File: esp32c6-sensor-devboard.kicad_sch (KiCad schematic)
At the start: 85 parts, among them J1 Conn_01x04_Pin, J2 Micro_SD_Card_Det1, J3 Screw_Terminal_01x02, J4 USB_C_Receptacle_USB2.0_14P, J5 Screw_Terminal_01x02, J6 Screw_Terminal_01x06, J7 Screw_Terminal_01x04, J8 Conn_01x04_Pin, J9 Conn_01x03_Pin, SW1 SW_Push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

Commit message: schem: assign footprints
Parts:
- AE1: footprint (none) -> RF_Antenna:Johanson_2450AT18x100
- C3: footprint (none) -> Capacitor_SMD:C_0603_1608Metric
- C48, C49, C50, C51: footprint (none) -> Capacitor_SMD:C_0402_1005Metric
- D10: footprint (none) -> LED_SMD:LED_0805_2012Metric
- D9: footprint (none) -> LED_SMD:LED_0603_1608Metric
- J1, J8: footprint (none) -> Connector_PinHeader_2.54mm:PinHeader_1x04_P2.54mm_Vertical
- J3, J5: footprint (none) -> TerminalBlock:TerminalBlock_Altech_AK300-2_P5.00mm
- J6: footprint (none) -> TerminalBlock_Phoenix:TerminalBlock_Phoenix_MKDS-1,5-6_1x06_P5.00mm_Horizontal
- J7: footprint (none) -> TerminalBlock:TerminalBlock_Altech_AK300-4_P5.00mm
- J9: footprint (none) -> Connector_PinHeader_2.54mm:PinHeader_1x03_P2.54mm_Vertical
- JP1: footprint (none) -> Connector_PinHeader_2.54mm:PinHeader_1x02_P2.54mm_Vertical
- R1, R2, R3, R4, R5, R57, R58, R59, R6, R60, R61, R62: footprint (none) -> Resistor_SMD:R_0603_1608Metric
- R10, R14, R16, R17, R18, R19, R20, R21, R22: footprint (none) -> Resistor_SMD:R_0402_1005Metric
- SW1, SW2: footprint Button_Switch_THT:SW_SPST_Omron_B3F-40xx -> Button_Switch_SMD:SW_SPST_TS-1088-xR020
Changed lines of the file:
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@@
 			)
 		)
-		(property "Footprint" ""
+		(property "Footprint" "TerminalBlock:TerminalBlock_Altech_AK300-2_P5.00mm"
 			(at 227.33 157.48 0)
 			(effects
@@
 			)
 		)
-		(property "Footprint" ""
+		(property "Footprint" "TerminalBlock:TerminalBlock_Altech_AK300-4_P5.00mm"
 			(at 275.59 143.51 0)
 			(effects
@@
 			)
 		)
-		(property "Footprint" ""
+		(property "Footprint" "Resistor_SMD:R_0603_1608Metric"
 			(at 48.26 97.028 90)
 			(effects
@@
 			)
 		)
-		(property "Footprint" ""
+		(property "Footprint" "Resistor_SMD:R_0603_1608Metric"
 			(at 222.25 99.568 90)
 			(effects
@@
 			)
 		)
-		(property "Footprint" ""
+		(property "Footprint" "Resistor_SMD:R_0603_1608Metric"
 			(at 270.002 27.94 90)
 			(effects
@@
 			)
 		)
-		(property "Footprint" ""
+		(property "Footprint" "Capacitor_SMD:C_0402_1005Metric"
 			(at 270.8148 69.85 0)
 			(effects
@@
 			)
 		)
-		(property "Footprint" ""
+		(property "Footprint" "Resistor_SMD:R_0402_1005Metric"
 			(at 135.89 148.082 90)
 			(effects
@@
 			)
 		)
-		(property "Footprint" ""
+		(property "Footprint" "Resistor_SMD:R_0603_1608Metric"
 			(at 222.25 94.488 90)
 			(effects
@@
 			)
 		)
-		(property "Footprint" "Button_Switch_THT:SW_SPST_Omron_B3F-40xx"
+		(property "Footprint" "Button_Switch_SMD:SW_SPST_TS-1088-xR020"
 			(at 26.67 180.34 0)
 			(effects
@@
 			)
 		)
-		(property "Footprint" ""
+		(property "Footprint" "Resistor_SMD:R_0603_1608Metric"
 			(at 48.26 107.188 90)
 			(effects
@@
 			)
 		)
-		(property "Footprint" ""
+		(property "Footprint" "Resistor_SMD:R_0402_1005Metric"
 			(at 135.89 145.542 90)
 			(effects
@@
 			)
 		)
-		(property "Footprint" ""
+		(property "Footprint" "Resistor_SMD:R_0402_1005Metric"
 			(at 143.51 65.532 90)
 			(effects
@@
 			)
 		)
-		(property "Footprint" ""
+		(property "Footprint" "Resistor_SMD:R_0603_1608Metric"
 			(at 246.38 83.058 90)
 			(effects
@@
 			)
 		)
-		(property "Footprint" ""
+		(property "Footprint" "Capacitor_SMD:C_0402_1005Metric"
 			(at 264.16 24.4348 0)
 			(effects
@@
 			)
 		)
-		(property "Footprint" ""
+		(property "Footprint" "Capacitor_SMD:C_0603_1608Metric"
 			(at 159.7152 165.1 0)
 			(effects
@@
 			)
 		)
-		(property "Footprint" ""
+		(property "Footprint" "Resistor_SMD:R_0603_1608Metric"
 			(at 154.432 132.08 90)
 			(effects
@@
 			)
 		)
-		(property "Footprint" ""
+		(property "Footprint" "Connector_PinHeader_2.54mm:PinHeader_1x03_P2.54mm_Vertical"
 			(at 63.5 118.11 0)
 			(effects
@@
 			)
 		)
-		(property "Footprint" ""
+		(property "Footprint" "Resistor_SMD:R_0402_1005Metric"
 			(at 135.89 150.622 90)
 			(effects
@@
 			)
 		)
-		(property "Footprint" ""
+		(property "Footprint" "Resistor_SMD:R_0402_1005Metric"
 			(at 143.51 66.548 90)
 			(effects
@@
 			)
 		)
-		(property "Footprint" ""
+		(property "Footprint" "Capacitor_SMD:C_0402_1005Metric"
 			(at 214.63 24.4348 0)
 			(effects
@@
 			)
 		)
-		(property "Footprint" "Button_Switch_THT:SW_SPST_Omron_B3F-40xx"
+		(property "Footprint" "Button_Switch_SMD:SW_SPST_TS-1088-xR020"
 			(at 26.67 173.99 0)
 			(effects
@@
 			)
 		)
-		(property "Footprint" ""
+		(property "Footprint" "Connector_PinHeader_2.54mm:PinHeader_1x02_P2.54mm_Vertical"
 			(at 121.92 129.54 0)
 			(effects
@@
 			)
 		)
-		(property "Footprint" ""
+		(property "Footprint" "TerminalBlock_Phoenix:TerminalBlock_Phoenix_MKDS-1,5-6_1x06_P5.00mm_Horizontal"
 			(at 270.51 125.73 0)
 			(effects
@@
 			)
 		)
-		(property "Footprint" ""
+		(property "Footprint" "Resistor_SMD:R_0603_1608Metric"
 			(at 48.26 94.488 90)
 			(effects
@@
 			)
 		)
-		(property "Footprint" ""
+		(property "Footprint" "Connector_PinHeader_2.54mm:PinHeader_1x04_P2.54mm_Vertical"
 			(at 60.96 82.55 0)
 			(effects
@@
 			)
 		)
-		(property "Footprint" ""
+		(property "Footprint" "Resistor_SMD:R_0402_1005Metric"
 			(at 135.89 143.002 90)
 			(effects
@@
 			)
 		)
-		(property "Footprint" ""
+		(property "Footprint" "Resistor_SMD:R_0603_1608Metric"
 			(at 220.472 27.94 90)
 			(effects
@@
 			)
 		)
-		(property "Footprint" ""
+		(property "Footprint" "Resistor_SMD:R_0603_1608Metric"
 			(at 48.26 104.648 90)
 			(effects
@@
 			)
 		)
-		(property "Footprint" ""
+		(property "Footprint" "Resistor_SMD:R_0603_1608Metric"
 			(at 48.26 99.568 90)
 			(effects
@@
 			)
 		)
-		(property "Footprint" ""
+		(property "Footprint" "RF_Antenna:Johanson_2450AT18x100"
 			(at 39.37 34.29 0)
 			(effects
@@
 			)
 		)
-		(property "Footprint" ""
+		(property "Footprint" "Resistor_SMD:R_0402_1005Metric"
 			(at 135.89 140.462 90)
 			(effects
@@
 			)
 		)
-		(property "Footprint" ""
+		(property "Footprint" "TerminalBlock:TerminalBlock_Altech_AK300-2_P5.00mm"
 			(at 199.39 140.97 0)
 			(effects
@@
 			)
 		)
-		(property "Footprint" ""
+		(property "Footprint" "LED_SMD:LED_0805_2012Metric"
 			(at 212.09 97.79 0)
 			(effects
@@
 			)
 		)
-		(property "Footprint" ""
+		(property "Footprint" "Resistor_SMD:R_0603_1608Metric"
 			(at 48.26 109.728 90)
 			(effects
@@
 			)
 		)
-		(property "Footprint" ""
+		(property "Footprint" "Connector_PinHeader_2.54mm:PinHeader_1x04_P2.54mm_Vertical"
 			(at 156.21 33.02 0)
 			(effects
@@
 			)
 		)
-		(property "Footprint" ""
+		(property "Footprint" "Resistor_SMD:R_0402_1005Metric"
 			(at 149.352 43.18 90)
 			(effects
@@
 			)
 		)
-		(property "Footprint" ""
+		(property "Footprint" "Resistor_SMD:R_0402_1005Metric"
 			(at 135.89 137.922 90)
 			(effects
@@
 			)
 		)
-		(property "Footprint" ""
+		(property "Footprint" "LED_SMD:LED_0603_1608Metric"
 			(at 212.09 92.71 0)
 			(effects
@@
 			)
 		)
-		(property "Footprint" ""
+		(property "Footprint" "Capacitor_SMD:C_0402_1005Metric"
 			(at 254 67.6148 0)
 			(effects

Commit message: schem: add part numbers to BOM
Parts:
- AE1: Basic (none) -> X; JLCPCB Part # (none) -> C89334; Manufacturer (none) -> Johanson Dielectrics; Manufacturer Part Number (none) -> 2450AT18A100E
- C3: Basic (none) -> Y; JLCPCB Part # (none) -> C14663; Manufacturer (none) -> YAGEO; Manufacturer Part Number (none) -> CC0603KRX7R9BB104
- C48, C49, C50, C51: Basic (none) -> Y; JLCPCB Part # (none) -> C307331; Manufacturer (none) -> Samsung Electro-Mechanics; Manufacturer Part Number (none) -> CL05B104KB54PNC
- D10: Basic (none) -> Y; JLCPCB Part # (none) -> C2297; Manufacturer (none) -> Hubei KENTO Elec; Manufacturer Part Number (none) -> KT-0805G
- D9: Basic (none) -> Y; JLCPCB Part # (none) -> C2286; Manufacturer (none) -> Hubei KENTO Elec; Manufacturer Part Number (none) -> KT-0603R
- J1, J3, J5, J6, J7, J8, J9, JP1: now left out of the parts list
- SW1, SW2, SW3: now in the parts list

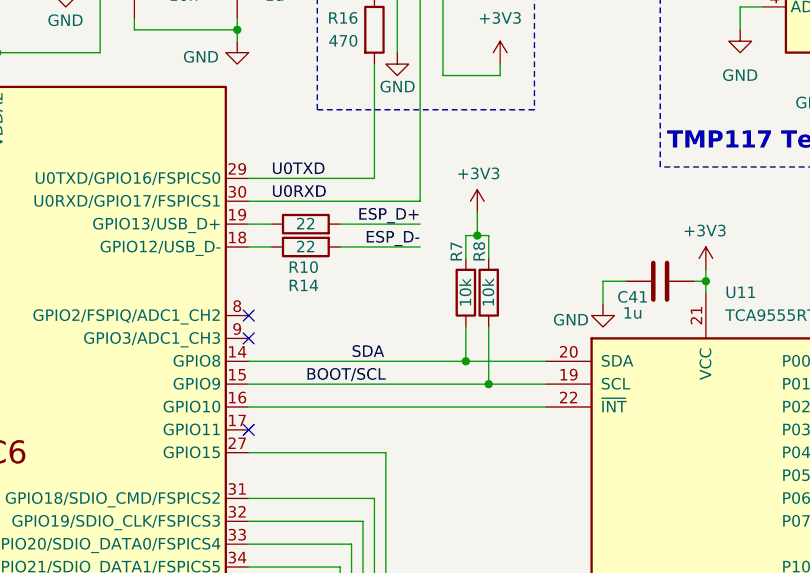
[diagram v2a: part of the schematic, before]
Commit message: schem: add PCA9555 interupt pin pull-up
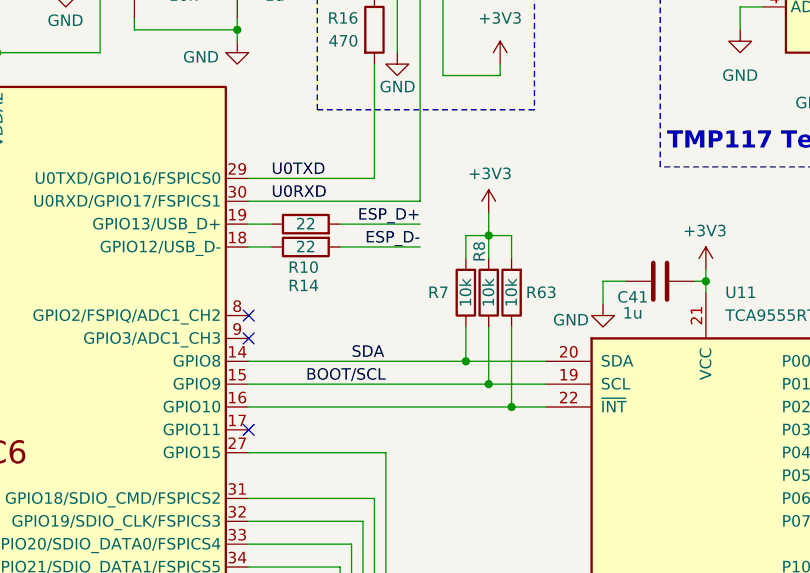
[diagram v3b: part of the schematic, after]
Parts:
- added R63: 10k, Resistor_SMD:R_0603_1608Metric, symbol Device:R
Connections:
- net +3V3: now also R63.2
- net at U1.16 (GPIO10), U11.22 (~{INT}): now also R63.1
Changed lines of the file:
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@@
 	)
 	(junction
-		(at 162.56 66.04)
-		(diameter 0)
-		(color 0 0 0 0)
-	)
-	(junction
 		(at 58.42 40.64)
 		(diameter 0)
@@
 	)
 	(junction
+		(at 166.37 85.09)
+		(diameter 0)
+		(color 0 0 0 0)
+	)
+	(junction
 		(at 43.18 154.94)
 		(diameter 0)
@@
 	)
 	(junction
+		(at 163.83 66.04)
+		(diameter 0)
+		(color 0 0 0 0)
+	)
+	(junction
 		(at 139.7 135.89)
 		(diameter 0)
@@
 	(wire
 		(pts
-			(xy 163.83 66.04) (xy 162.56 66.04)
-		)
-		(stroke
-			(width 0)
-			(type default)
-		)
-	)
-	(wire
-		(pts
 			(xy 60.96 157.48) (xy 72.39 157.48)
 		)
@@
 	(wire
 		(pts
-			(xy 162.56 66.04) (xy 161.29 66.04)
+			(xy 161.29 66.04) (xy 163.83 66.04)
 		)
 		(stroke
@@
 	(wire
 		(pts
+			(xy 166.37 85.09) (xy 170.18 85.09)
+		)
+		(stroke
+			(width 0)
+			(type default)
+		)
+	)
+	(wire
+		(pts
 			(xy 68.58 24.13) (xy 68.58 25.4)
 		)
@@
 	(wire
 		(pts
+			(xy 166.37 68.58) (xy 166.37 66.04)
+		)
+		(stroke
+			(width 0)
+			(type default)
+		)
+	)
+	(wire
+		(pts
 			(xy 241.3 83.82) (xy 251.46 83.82)
 		)
@@
 	(wire
 		(pts
+			(xy 166.37 66.04) (xy 163.83 66.04)
+		)
+		(stroke
+			(width 0)
+			(type default)
+		)
+	)
+	(wire
+		(pts
 			(xy 156.21 135.89) (xy 156.21 139.7)
 		)
@@
 	(wire
 		(pts
-			(xy 137.16 85.09) (xy 170.18 85.09)
+			(xy 137.16 85.09) (xy 166.37 85.09)
 		)
 		(stroke
@@
 	(wire
 		(pts
+			(xy 166.37 76.2) (xy 166.37 85.09)
+		)
+		(stroke
+			(width 0)
+			(type default)
+		)
+	)
+	(wire
+		(pts
 			(xy 38.1 97.79) (xy 44.45 97.79)
 		)
@@
 	(wire
 		(pts
-			(xy 162.56 63.5) (xy 162.56 66.04)
+			(xy 163.83 63.5) (xy 163.83 66.04)
 		)
 		(stroke
@@
 	(symbol
 		(lib_id "power:+3V3")
-		(at 162.56 63.5 0)
+		(at 163.83 63.5 0)
 		(unit 1)
 		(exclude_from_sim no)
@@
 		(dnp no)
 		(property "Reference" "#PWR03"
-			(at 162.56 67.31 0)
+			(at 163.83 67.31 0)
 			(effects
 				(font
@@
 		)
 		(property "Value" "+3V3"
-			(at 160.274 59.182 0)
+			(at 161.544 59.182 0)
 			(effects
 				(font
@@
 		)
 		(property "Footprint" ""
-			(at 162.56 63.5 0)
+			(at 163.83 63.5 0)
 			(effects
 				(font
@@
 		)
 		(property "Datasheet" ""
-			(at 162.56 63.5 0)
+			(at 163.83 63.5 0)
 			(effects
 				(font
@@
 		)
 		(property "Description" "Power symbol creates a global label with name \"+3V3\""
-			(at 162.56 63.5 0)
+			(at 163.83 63.5 0)
 			(effects
 				(font
@@
 	)
 	(symbol
+		(lib_id "Device:R")
+		(at 166.37 72.39 180)
+		(unit 1)
+		(exclude_from_sim no)
+		(in_bom yes)
+		(on_board yes)
+		(dnp no)
+		(property "Reference" "R63"
+			(at 169.672 72.39 0)
+			(effects
+				(font
+					(size 1.27 1.27)
+				)
+			)
+		)
+		(property "Value" "10k"
+			(at 166.37 72.39 90)
+			(effects
+				(font
+					(size 1.27 1.27)
+				)
+			)
+		)
+		(property "Footprint" "Resistor_SMD:R_0603_1608Metric"
+			(at 168.148 72.39 90)
+			(effects
+				(font
+					(size 1.27 1.27)
+				)
+				(hide yes)
+			)
+		)
+		(property "Datasheet" "~"
+			(at 166.37 72.39 0)
+			(effects
+				(font
+					(size 1.27 1.27)
+				)
+				(hide yes)
+			)
+		)
+		(property "Description" "Resistor"
+			(at 166.37 72.39 0)
+			(effects
+				(font
+					(size 1.27 1.27)
+				)
+				(hide yes)
+			)
+		)
+		(property "Manufacturer" "Uniroyal Elec"
+			(at 166.37 72.39 0)
+			(effects
+				(font
+					(size 1.27 1.27)
+				)
+				(hide yes)
+			)
+		)
+		(property "Manufacturer Part Number" "0603WAF1002T5E"
+			(at 166.37 72.39 0)
+			(effects
+				(font
+					(size 1.27 1.27)
+				)
+				(hide yes)
+			)
+		)
+		(property "Basic" "Y"
+			(at 166.37 72.39 0)
+			(effects
+				(font
+					(size 1.27 1.27)
+				)
+				(hide yes)
+			)
+		)
+		(property "JLCPCB Part #" "C25804"
+			(at 166.37 72.39 0)
+			(effects
+				(font
+					(size 1.27 1.27)
+				)
+				(hide yes)
+			)
+		)
+		(pin "1"
+		)
+		(pin "2"
+		)
+		(instances
+			(project "esp32c6-sensor-devboard"
+				(path "/f6edeef8-7fa0-4f55-9ad8-145372f41e3e"
+					(reference "R63")
+					(unit 1)
+				)
+			)
+		)
+	)
+	(symbol
 		(lib_id "power:+3V3")
 		(at 264.16 64.77 0)
@@
 		(dnp no)
 		(property "Reference" "R7"
-			(at 160.274 67.818 90)
+			(at 158.242 72.39 0)
 			(effects
 				(font

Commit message: schem: add remaining part numbers to BOM
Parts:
- J2: footprint Connector_Card:microSD_HC_Molex_47219-2001 -> Pers:microSD_Hanbo_TF012; Basic (none) -> X; JLCPCB Part # (none) -> C410350; Manufacturer (none) -> Hanbo Electronic; Manufacturer Part Number (none) -> TF-012
- R1, R2, R3, R4, R5, R6: footprint Resistor_SMD:R_0603_1608Metric -> Resistor_SMD:R_0402_1005Metric; Basic (none) -> Y; JLCPCB Part # (none) -> C17168; Manufacturer (none) -> Uniroyal Elec; Manufacturer Part Number (none) -> 0402WGF0000TCE
- R10, R14, R17, R18, R19, R20, R21, R22: Basic (none) -> Y; JLCPCB Part # (none) -> C25092; Manufacturer (none) -> Uniroyal Elec; Manufacturer Part Number (none) -> 0402WGF220JTCE
- R16: Basic (none) -> Y; JLCPCB Part # (none) -> C25117; Manufacturer (none) -> Uniroyal Elec; Manufacturer Part Number (none) -> 0402WGF4700TCE
- R57, R58, R61, R62: Basic (none) -> Y; JLCPCB Part # (none) -> C25804; Manufacturer (none) -> Uniroyal Elec; Manufacturer Part Number (none) -> 0603WAF1002T5E
- R59, R60: Basic (none) -> Y; JLCPCB Part # (none) -> C23186; Manufacturer (none) -> Uniroyal Elec; Manufacturer Part Number (none) -> 0603WAF5101T5E
- SW1, SW2: Basic (none) -> Y; JLCPCB Part # (none) -> C720477; Manufacturer (none) -> XUNPU; Manufacturer Part Number (none) -> TS-1088-AR02016
- SW3: now left out of the parts list
- U1: Basic (none) -> X; JLCPCB Part # (none) -> C5364646; Manufacturer (none) -> Espressif Systems; Manufacturer Part Number (none) -> ESP32-C6
- U11: Basic (none) -> X; JLCPCB Part # (none) -> C140277; Manufacturer (none) -> Texas Instruments; Manufacturer Part Number (none) -> TCA9555RTWR
- U14, U16: Basic (none) -> X; JLCPCB Part # (none) -> C699536; Manufacturer (none) -> Texas Instruments; Manufacturer Part Number (none) -> TMP117AIDRVR
- U15: Basic (none) -> X; JLCPCB Part # (none) -> C5362283; Manufacturer (none) -> Bosch Sensortec; Manufacturer Part Number (none) -> BMP581
- U2: Basic (none) -> Y; JLCPCB Part # (none) -> C97521; Manufacturer (none) -> Winbond Elec; Manufacturer Part Number (none) -> W25Q128JVSIQ

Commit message: schem: fix UBS C receptacle hidden power pins
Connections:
- net GND: now also J4.A12 (GND), J4.B1 (GND), J4.B12 (GND)
- net VBUS: now also J4.A9 (VBUS), J4.B4 (VBUS), J4.B9 (VBUS)

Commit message: pcb: add missing 3d models
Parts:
- U11: footprint Package_DFN_QFN:WQFN-24-1EP_4x4mm_P0.5mm_EP2.45x2.45mm -> Package_DFN_QFN:Texas_RTW_WQFN-24-1EP_4x4mm_P0.5mm_EP2.7x2.7mm_ThermalVias
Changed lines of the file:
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@@
 			)
 		)
-		(property "Footprint" "Package_DFN_QFN:WQFN-24-1EP_4x4mm_P0.5mm_EP2.45x2.45mm"
+		(property "Footprint" "Package_DFN_QFN:Texas_RTW_WQFN-24-1EP_4x4mm_P0.5mm_EP2.7x2.7mm_ThermalVias"
 			(at 218.44 125.73 0)
 			(effects

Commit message: pcb: initial rough pcb placement
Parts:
- R23, R24, R25, R26, R27: footprint Resistor_SMD:R_0603_1608Metric -> Resistor_SMD:R_0402_1005Metric; JLCPCB Part # C25804 -> C25744; Manufacturer Part Number 0603WAF1002T5E -> 0402WGF1002TCE
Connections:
- net ESP_D-: no longer R14.2
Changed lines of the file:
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@@
 		)
 	)
-	(label "ESP_D-"
-		(at 156.21 67.31 180)
-		(effects
-			(font
-				(size 1.27 1.27)
-			)
-			(justify right bottom)
-		)
-	)
 	(rule_area
 		(polyline
@@
 			)
 		)
-		(property "Footprint" "Resistor_SMD:R_0603_1608Metric"
+		(property "Footprint" "Resistor_SMD:R_0402_1005Metric"
 			(at 138.938 129.54 90)
 			(effects
@@
 			)
 		)
-		(property "Manufacturer Part Number" "0603WAF1002T5E"
+		(property "Manufacturer Part Number" "0402WGF1002TCE"
 			(at 137.16 129.54 0)
 			(effects
@@
 			)
 		)
-		(property "JLCPCB Part #" "C25804"
+		(property "JLCPCB Part #" "C25744"
 			(at 137.16 129.54 0)
 			(effects
@@
 		(on_board yes)
 		(dnp no)
+		(fields_autoplaced yes)
 		(property "Reference" "R21"
 			(at 140.208 148.844 90)
@@
 		(on_board yes)
 		(dnp no)
+		(fields_autoplaced yes)
 		(property "Reference" "R20"
 			(at 140.208 146.304 90)
@@
 			)
 		)
-		(property "Footprint" "Resistor_SMD:R_0603_1608Metric"
+		(property "Footprint" "Resistor_SMD:R_0402_1005Metric"
 			(at 144.018 129.54 90)
 			(effects
@@
 			)
 		)
-		(property "Manufacturer Part Number" "0603WAF1002T5E"
+		(property "Manufacturer Part Number" "0402WGF1002TCE"
 			(at 142.24 129.54 0)
 			(effects
@@
 			)
 		)
-		(property "JLCPCB Part #" "C25804"
+		(property "JLCPCB Part #" "C25744"
 			(at 142.24 129.54 0)
 			(effects
@@
 		(on_board yes)
 		(dnp no)
+		(fields_autoplaced yes)
 		(property "Reference" "R22"
 			(at 140.208 151.384 90)
@@
 		(on_board yes)
 		(dnp no)
+		(fields_autoplaced yes)
 		(property "Reference" "R19"
 			(at 140.208 143.764 90)
@@
 		(on_board yes)
 		(dnp no)
+		(fields_autoplaced yes)
 		(property "Reference" "R18"
 			(at 140.208 141.224 90)
@@
 			)
 		)
-		(property "Footprint" "Resistor_SMD:R_0603_1608Metric"
+		(property "Footprint" "Resistor_SMD:R_0402_1005Metric"
 			(at 141.478 129.54 90)
 			(effects
@@
 			)
 		)
-		(property "Manufacturer Part Number" "0603WAF1002T5E"
+		(property "Manufacturer Part Number" "0402WGF1002TCE"
 			(at 139.7 129.54 0)
 			(effects
@@
 			)
 		)
-		(property "JLCPCB Part #" "C25804"
+		(property "JLCPCB Part #" "C25744"
 			(at 139.7 129.54 0)
 			(effects
@@
 		(on_board yes)
 		(dnp no)
+		(fields_autoplaced yes)
 		(property "Reference" "R17"
 			(at 140.208 138.684 90)
@@
 			)
 		)
-		(property "Footprint" "Resistor_SMD:R_0603_1608Metric"
+		(property "Footprint" "Resistor_SMD:R_0402_1005Metric"
 			(at 136.398 129.54 90)
 			(effects
@@
 			)
 		)
-		(property "Manufacturer Part Number" "0603WAF1002T5E"
+		(property "Manufacturer Part Number" "0402WGF1002TCE"
 			(at 134.62 129.54 0)
 			(effects
@@
 			)
 		)
-		(property "JLCPCB Part #" "C25804"
+		(property "JLCPCB Part #" "C25744"
 			(at 134.62 129.54 0)
 			(effects
@@
 			)
 		)
-		(property "Footprint" "Resistor_SMD:R_0603_1608Metric"
+		(property "Footprint" "Resistor_SMD:R_0402_1005Metric"
 			(at 133.858 129.54 90)
 			(effects
@@
 			)
 		)
-		(property "Manufacturer Part Number" "0603WAF1002T5E"
+		(property "Manufacturer Part Number" "0402WGF1002TCE"
 			(at 132.08 129.54 0)
 			(effects
@@
 			)
 		)
-		(property "JLCPCB Part #" "C25804"
+		(property "JLCPCB Part #" "C25744"
 			(at 132.08 129.54 0)
 			(effects

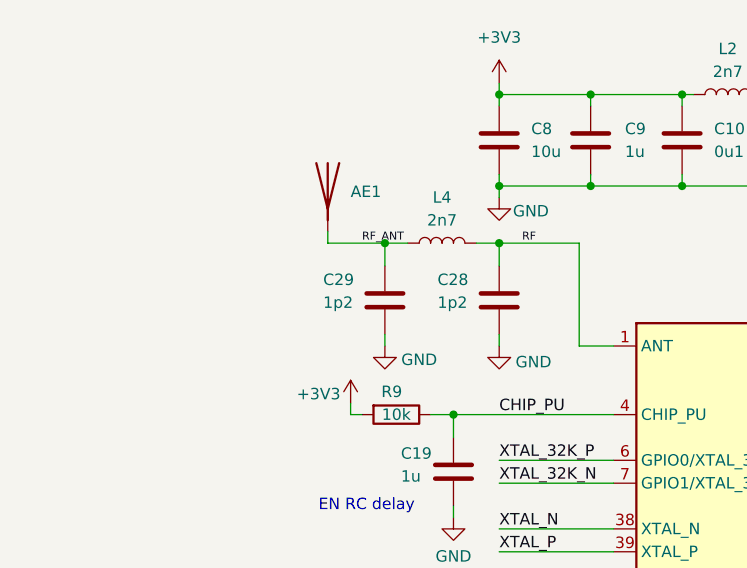
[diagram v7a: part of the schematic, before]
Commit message: schem/pcb: add antenna matching network
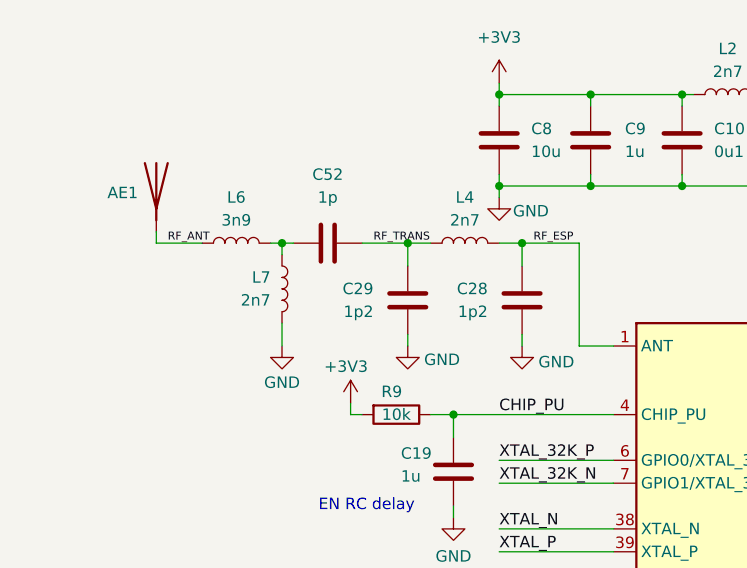
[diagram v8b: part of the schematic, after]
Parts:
- added C52: 1p, Capacitor_SMD:C_0402_1005Metric, symbol Device:C
- added L6: 3n9, Inductor_SMD:L_0402_1005Metric, symbol Device:L
- added L7: 2n7, Inductor_SMD:L_0402_1005Metric, symbol Device:L
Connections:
- net GND: now also L7.1
- net RF_ANT: now also L6.1; no longer C29.1, L4.1
- net RF renamed RF_ESP
- new net: C52.2, L6.2, L7.2
- new net RF_TRANS: C29.1, C52.1, L4.1
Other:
- moved on the sheet: AE1, C28, C29, L4
